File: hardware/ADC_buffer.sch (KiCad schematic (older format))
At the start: 60 parts, among them J16 TBA1E, J7 JMP_A0, U6 THS4032ID, U7 THS4551IDGKT, U8 THS4551IDGKT

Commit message: Finishing routing
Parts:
- added C15, C16: 330n, Capacitor_SMD:C_0603_1608Metric, symbol antena:C
- added C40, C41: 100n, Capacitor_SMD:C_0603_1608Metric, symbol antena:C
- added C42, C43, C44, C45: 10u, Capacitor_SMD:C_0603_1608Metric, symbol antena:C
- added L2, L3: L, Capacitor_SMD:C_0603_1608Metric, symbol antena:L
- added U5: MC78L05_SO8, Package_SO:SOIC-8_3.9x4.9mm_P1.27mm, symbol Regulator_Linear:MC78L05_SO8
- added U9: MC79L05_SO8, Package_SO:SOIC-8_3.9x4.9mm_P1.27mm, symbol Regulator_Linear:MC79L05_SO8
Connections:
- net AGND is gone; now on net GND: C30.2, C31.2, C32.2, C36.2, D2.2 (A2), D3.2 (A2), D4.2 (A2), D5.2 (A2), D6.2 (A2), D7.2 (A2), R25.1, R50.2, R54.2, U7.6 (VS-), U8.6 (VS-)
- net GND: now also C15.2, C16.2, C40.2, C41.2, C42.2, C43.2, C44.2, C45.2
- net HVDD: now also C44.1, L2.2; no longer J16.6 (+Vout)
- net HVSS: now also C45.1, L3.2; no longer J16.4 (–Vout)
- new net: C40.1, C42.1, L2.1, U5.1 (OUT)
- new net: U5.2 (GND), U5.3 (GND), U5.6 (GND), U5.7 (GND), U9.5 (GND)
- new net: C41.1, C43.1, L3.1, U9.1 (OUT)
- new net HVDD_9V: C15.1, J16.6 (+Vout), U5.8 (IN)
- new net HVSS_9V: C16.1, J16.4 (–Vout), U9.2 (IN), U9.3 (IN), U9.6 (IN), U9.7 (IN)
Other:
- note added: "+9V"
- note added: "-9V"
- note removed: "+5V"
- note removed: "-5V"
- moved on the sheet: C37, D5, R51, R52, R54

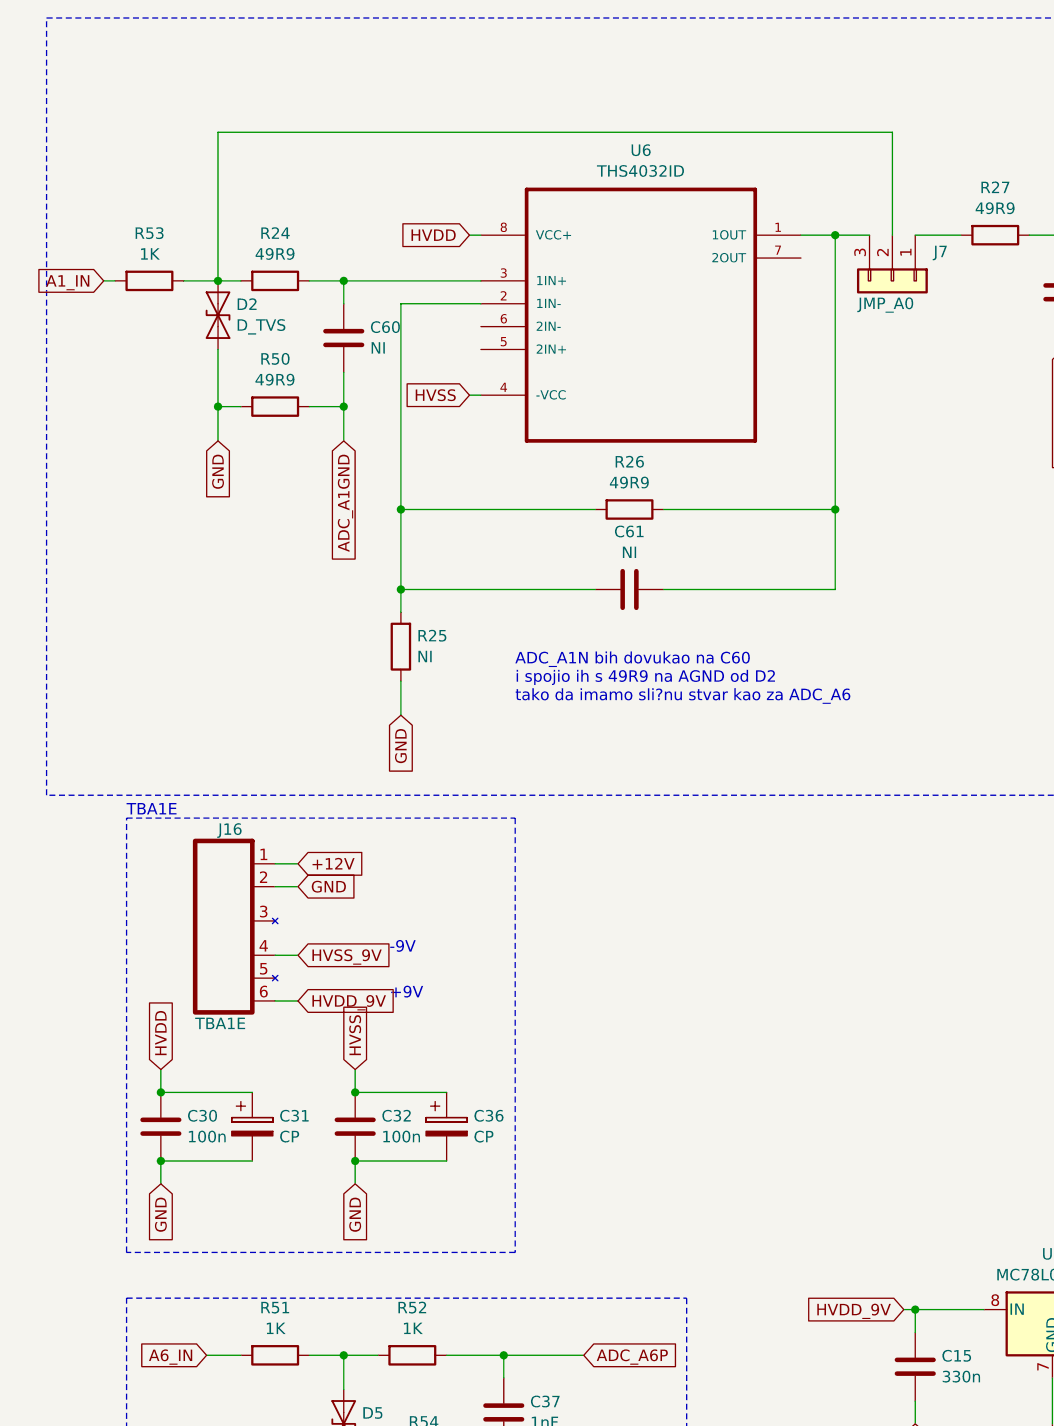
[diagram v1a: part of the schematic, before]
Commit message: Adding pcb changes to PBC
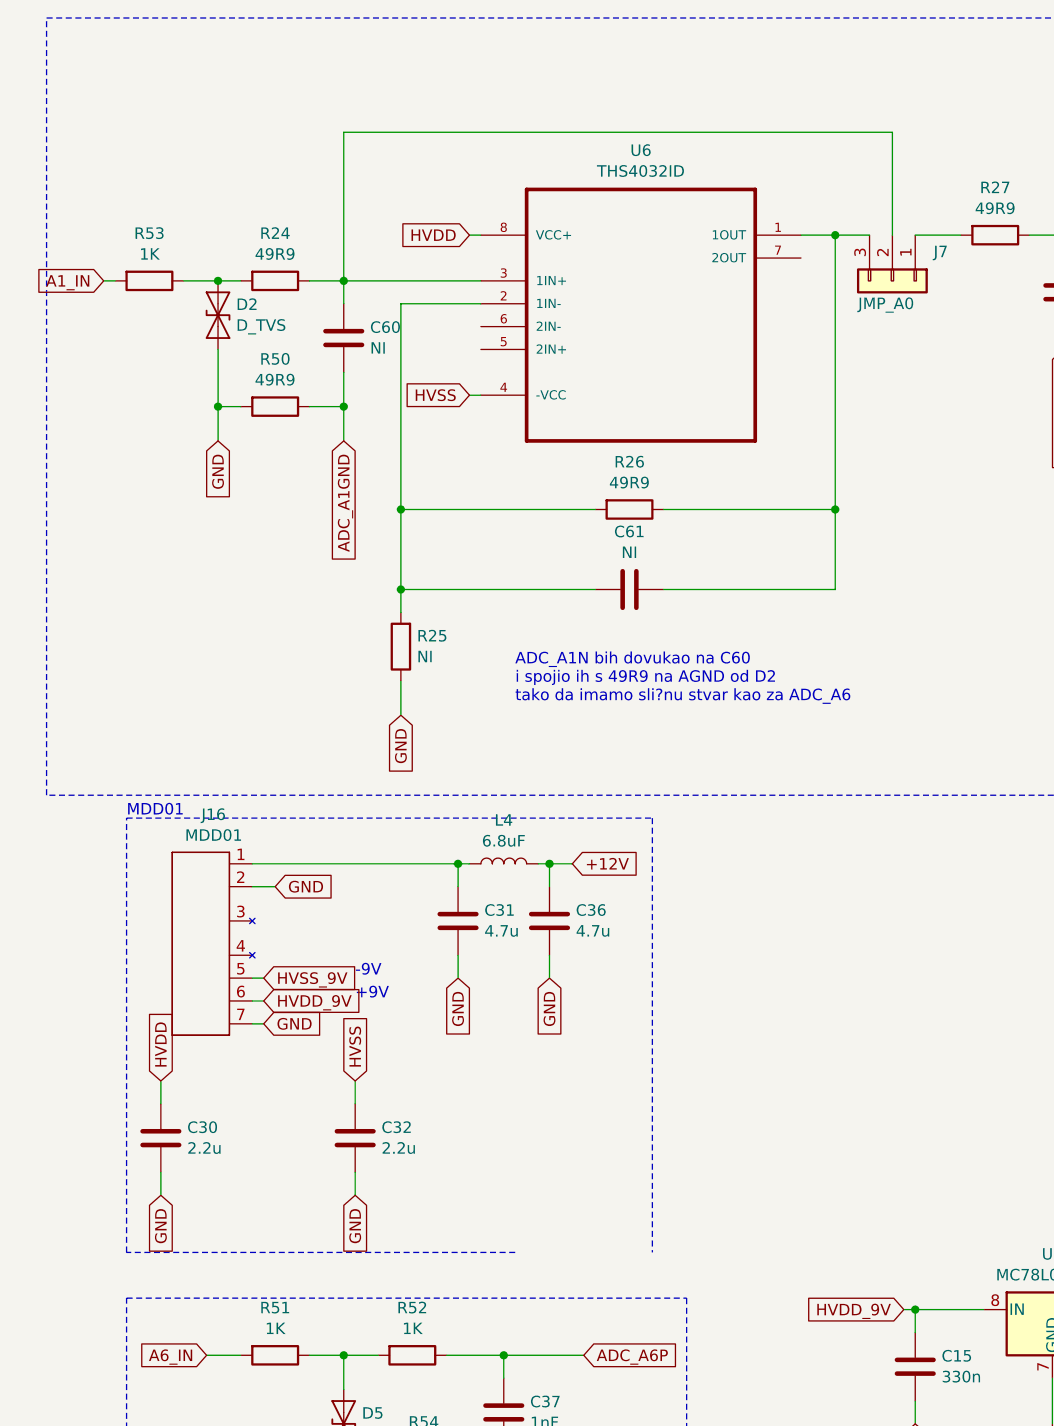
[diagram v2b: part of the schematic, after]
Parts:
- removed C31: CP, Capacitor_SMD:C_0805_2012Metric, symbol antena:CP
- removed C36: CP, Capacitor_Tantalum_SMD:CP_EIA-3528-21_Kemet-B, symbol antena:CP
- removed J16: TBA1E, TBA1E:TBA1E, symbol TBA1E:TBA1E
- added C31, C36: 4.7u, Capacitor_SMD:C_0603_1608Metric, symbol antena:C
- added J16: MDD01, MDS01:MDS01, symbol MDD01:MDD01
- added L4: 6.8uF, Resistor_SMD:R_0603_1608Metric, symbol antena:L
- C30, C32: value 100n -> 2.2u
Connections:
- net +12V: now also C36.1, L4.2
- net GND: now also C31.2, C36.2, J16.2 (–Vin_(GND)), J16.7 (Common)
- net HVDD_9V: now also J16.6 (+Vout)
- net HVSS_9V: now also J16.5 (-Vout)
- net at D2.1 (A1), R24.2, R53.1: no longer J7.2 (Pin_2)
- net at C60.1, R24.1, U6.3 (1IN+): now also J7.2 (Pin_2)
- new net: C31.1, J16.1 (+Vin_(Vcc)), L4.1
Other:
- note added: "MDD01"
- note removed: "TBA1E"
- moved on the sheet: C30, C32
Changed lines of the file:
@@
 Connection ~ 1800 1650
-Wire Wire Line
-	1250 1650 1250 1000
-Wire Wire Line
-	1250 1000 4200 1000
 Wire Wire Line
 	4200 1000 4200 1450
@@
 L antena:C C?
 U 1 1 5E63E862
-P 1000 5350
+P 1000 5400
 AR Path="/5E22D897/5E63E862" Ref="C?"  Part="1"
 AR Path="/5E22D897/5E785EBD/5E63E862" Ref="C30"  Part="1"
-F 0 "C30" H 1115 5396 50  0000 L CNN
-F 1 "100n" H 1115 5305 50  0000 L CNN
-F 2 "Capacitor_SMD:C_0603_1608Metric" H 1038 5200 50  0001 C CNN
-F 3 "~" H 1000 5350 50  0001 C CNN
-	1    1000 5350
+F 0 "C30" H 1115 5446 50  0000 L CNN
+F 1 "2.2u" H 1115 5355 50  0000 L CNN
+F 2 "Capacitor_SMD:C_0603_1608Metric" H 1038 5250 50  0001 C CNN
+F 3 "~" H 1000 5400 50  0001 C CNN
+	1    1000 5400
 	1    0    0    -1
 $EndComp
@@
 L antena:C C?
 U 1 1 5E63E869
-P 1850 5350
+P 1850 5400
 AR Path="/5E22D897/5E63E869" Ref="C?"  Part="1"
 AR Path="/5E22D897/5E785EBD/5E63E869" Ref="C32"  Part="1"
-F 0 "C32" H 1965 5396 50  0000 L CNN
-F 1 "100n" H 1965 5305 50  0000 L CNN
-F 2 "Capacitor_SMD:C_0603_1608Metric" H 1888 5200 50  0001 C CNN
-F 3 "~" H 1850 5350 50  0001 C CNN
-	1    1850 5350
-	1    0    0    -1
-$EndComp
-Text GLabel 1000 5600 3    50   Input ~ 0
-GND
-Text GLabel 1850 5600 3    50   Input ~ 0
-GND
-Text GLabel 1000 5100 1    50   Input ~ 0
+F 0 "C32" H 1965 5446 50  0000 L CNN
+F 1 "2.2u" H 1965 5355 50  0000 L CNN
+F 2 "Capacitor_SMD:C_0603_1608Metric" H 1888 5250 50  0001 C CNN
+F 3 "~" H 1850 5400 50  0001 C CNN
+	1    1850 5400
+	1    0    0    -1
+$EndComp
+Text GLabel 1000 5650 3    50   Input ~ 0
+GND
+Text GLabel 1850 5650 3    50   Input ~ 0
+GND
+Text GLabel 1000 5150 1    50   Input ~ 0
 HVDD
-Text GLabel 1850 5100 1    50   Input ~ 0
+Text GLabel 1850 5150 1    50   Input ~ 0
 HVSS
 Wire Wire Line
-	1000 5200 1400 5200
-Wire Wire Line
-	1400 5500 1000 5500
-Wire Wire Line
-	1000 5100 1000 5200
-Connection ~ 1000 5200
-Wire Wire Line
-	1000 5500 1000 5600
-Connection ~ 1000 5500
-Wire Wire Line
-	1850 5100 1850 5200
-Wire Wire Line
-	1850 5500 1850 5600
-Wire Wire Line
-	2250 5200 1850 5200
-Connection ~ 1850 5200
-Wire Wire Line
-	2250 5500 1850 5500
-Connection ~ 1850 5500
-Text Notes 2000 4600 0    50   ~ 0
+	1000 5150 1000 5250
+Wire Wire Line
+	1000 5550 1000 5650
+Wire Wire Line
+	1850 5150 1850 5250
+Wire Wire Line
+	1850 5550 1850 5650
+Text Notes 1850 4700 0    50   ~ 0
 -9V
-Text Notes 2000 4800 0    50   ~ 0
+Text Notes 1850 4800 0    50   ~ 0
 +9V
-Text GLabel 1600 4200 2    50   Input ~ 0
-+12V
-Text GLabel 1600 4300 2    50   Input ~ 0
-GND
-Text GLabel 1600 4600 2    50   Input ~ 0
+Text GLabel 1500 4300 2    50   Input ~ 0
+GND
+Text GLabel 1450 4700 2    50   Input ~ 0
 HVSS_9V
-Text GLabel 1600 4800 2    50   Input ~ 0
+Text GLabel 1450 4800 2    50   Input ~ 0
 HVDD_9V
 Text GLabel 1200 6350 0    50   Input ~ 0
@@
 Wire Wire Line
 	1800 6850 2000 6850
-$Comp
-L antena:CP C36
-U 1 1 5E715A92
-P 2250 5350
-F 0 "C36" H 2368 5396 50  0000 L CNN
-F 1 "CP" H 2368 5305 50  0000 L CNN
-F 2 "Capacitor_Tantalum_SMD:CP_EIA-3528-21_Kemet-B" H 2288 5200 50  0001 C CNN
-F 3 "~" H 2250 5350 50  0001 C CNN
-	1    2250 5350
-	1    0    0    -1
-$EndComp
-$Comp
-L antena:CP C31
-U 1 1 5E715B78
-P 1400 5350
-F 0 "C31" H 1518 5396 50  0000 L CNN
-F 1 "CP" H 1518 5305 50  0000 L CNN
-F 2 "Capacitor_SMD:C_0805_2012Metric" H 1438 5200 50  0001 C CNN
-F 3 "~" H 1400 5350 50  0001 C CNN
-	1    1400 5350
-	1    0    0    -1
-$EndComp
-Wire Notes Line
-	850  4000 2550 4000
-Wire Notes Line
-	2550 4000 2550 5900
+Wire Notes Line
+	3150 4000 3150 5900
 Wire Notes Line
 	2550 5900 850  5900
@@
 	850  5900 850  4000
 Text Notes 850  4000 0    50   ~ 0
-TBA1E
+MDD01
 Wire Notes Line
 	850  6100 3300 6100
@@
 	11200 500  5700 500
 $Comp
-L TBA1E:TBA1E J16
-U 1 1 5E4096F0
-P 350 6350
-F 0 "J16" V -1950 7250 50  0000 L CNN
-F 1 "TBA1E" V -1100 7150 50  0000 L CNN
-F 2 "TBA1E:TBA1E" V -1650 7950 50  0001 C CNN
-F 3 "~" V -1650 7950 50  0001 C CNN
-	1    350  6350
-	0    1    1    0
-$EndComp
-Wire Wire Line
-	1500 4200 1600 4200
-Wire Wire Line
-	1600 4300 1500 4300
-Wire Wire Line
-	1500 4600 1600 4600
-Wire Wire Line
-	1500 4800 1600 4800
-$Comp
 L Regulator_Linear:MC78L05_SO8 U5
 U 1 1 5E435E53
@@
 Wire Wire Line
 	5750 7450 5750 7350
+Wire Wire Line
+	4200 1000 1800 1000
+Wire Wire Line
+	1800 1000 1800 1650
+$Comp
+L MDD01:MDD01 J16
+U 1 1 5E4D591E
+P 250 6400
+F 0 "J16" V -2165 7381 50  0000 C CNN
+F 1 "MDD01" V -2074 7381 50  0000 C CNN
+F 2 "MDS01:MDS01" V -1750 8000 50  0001 C CNN
+F 3 "~" V -1750 8000 50  0001 C CNN
+	1    250  6400
+	0    1    1    0
+$EndComp
+Text GLabel 1450 4900 2    50   Input ~ 0
+GND
+Wire Wire Line
+	1400 4300 1500 4300
+Wire Wire Line
+	1400 4700 1450 4700
+Wire Wire Line
+	1400 4800 1450 4800
+Wire Wire Line
+	1400 4900 1450 4900
+$Comp
+L antena:C C?
+U 1 1 5E54A12F
+P 2300 4450
+AR Path="/5E22D897/5E54A12F" Ref="C?"  Part="1"
+AR Path="/5E22D897/5E785EBD/5E54A12F" Ref="C31"  Part="1"
+F 0 "C31" H 2415 4496 50  0000 L CNN
+F 1 "4.7u" H 2415 4405 50  0000 L CNN
+F 2 "Capacitor_SMD:C_0603_1608Metric" H 2338 4300 50  0001 C CNN
+F 3 "~" H 2300 4450 50  0001 C CNN
+	1    2300 4450
+	1    0    0    -1
+$EndComp
+$Comp
+L antena:C C?
+U 1 1 5E54A3F0
+P 2700 4450
+AR Path="/5E22D897/5E54A3F0" Ref="C?"  Part="1"
+AR Path="/5E22D897/5E785EBD/5E54A3F0" Ref="C36"  Part="1"
+F 0 "C36" H 2815 4496 50  0000 L CNN
+F 1 "4.7u" H 2815 4405 50  0000 L CNN
+F 2 "Capacitor_SMD:C_0603_1608Metric" H 2738 4300 50  0001 C CNN
+F 3 "~" H 2700 4450 50  0001 C CNN
+	1    2700 4450
+	1    0    0    -1
+$EndComp
+Text GLabel 2800 4200 2    50   Input ~ 0
++12V
+Wire Wire Line
+	2300 4300 2300 4200
+Wire Wire Line
+	1400 4200 2300 4200
+Text GLabel 2300 4700 3    50   Input ~ 0
+GND
+Text GLabel 2700 4700 3    50   Input ~ 0
+GND
+Wire Wire Line
+	2700 4700 2700 4600
+Wire Wire Line
+	2300 4700 2300 4600
+$Comp
+L antena:L L4
+U 1 1 5E5B56F2
+P 2500 4200
+F 0 "L4" V 2690 4200 50  0000 C CNN
+F 1 "6.8uF" V 2599 4200 50  0000 C CNN
+F 2 "Resistor_SMD:R_0603_1608Metric" H 2500 4200 50  0001 C CNN
+F 3 "~" H 2500 4200 50  0001 C CNN
+	1    2500 4200
+	0    -1   -1   0
+$EndComp
+Wire Wire Line
+	2650 4200 2700 4200
+Wire Wire Line
+	2350 4200 2300 4200
+Connection ~ 2300 4200
+Wire Wire Line
+	2700 4200 2700 4300
+Connection ~ 2700 4200
+Wire Wire Line
+	2700 4200 2800 4200
+Wire Notes Line
+	850  4000 3150 4000
 $EndSCHEMATC
